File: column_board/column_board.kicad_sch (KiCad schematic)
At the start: 17 parts, among them J1 Bus_M.2_Socket_B, J10 USB_C_Receptacle_PowerOnly_6P, U1 CH32V30xRxTx, Y1 Crystal

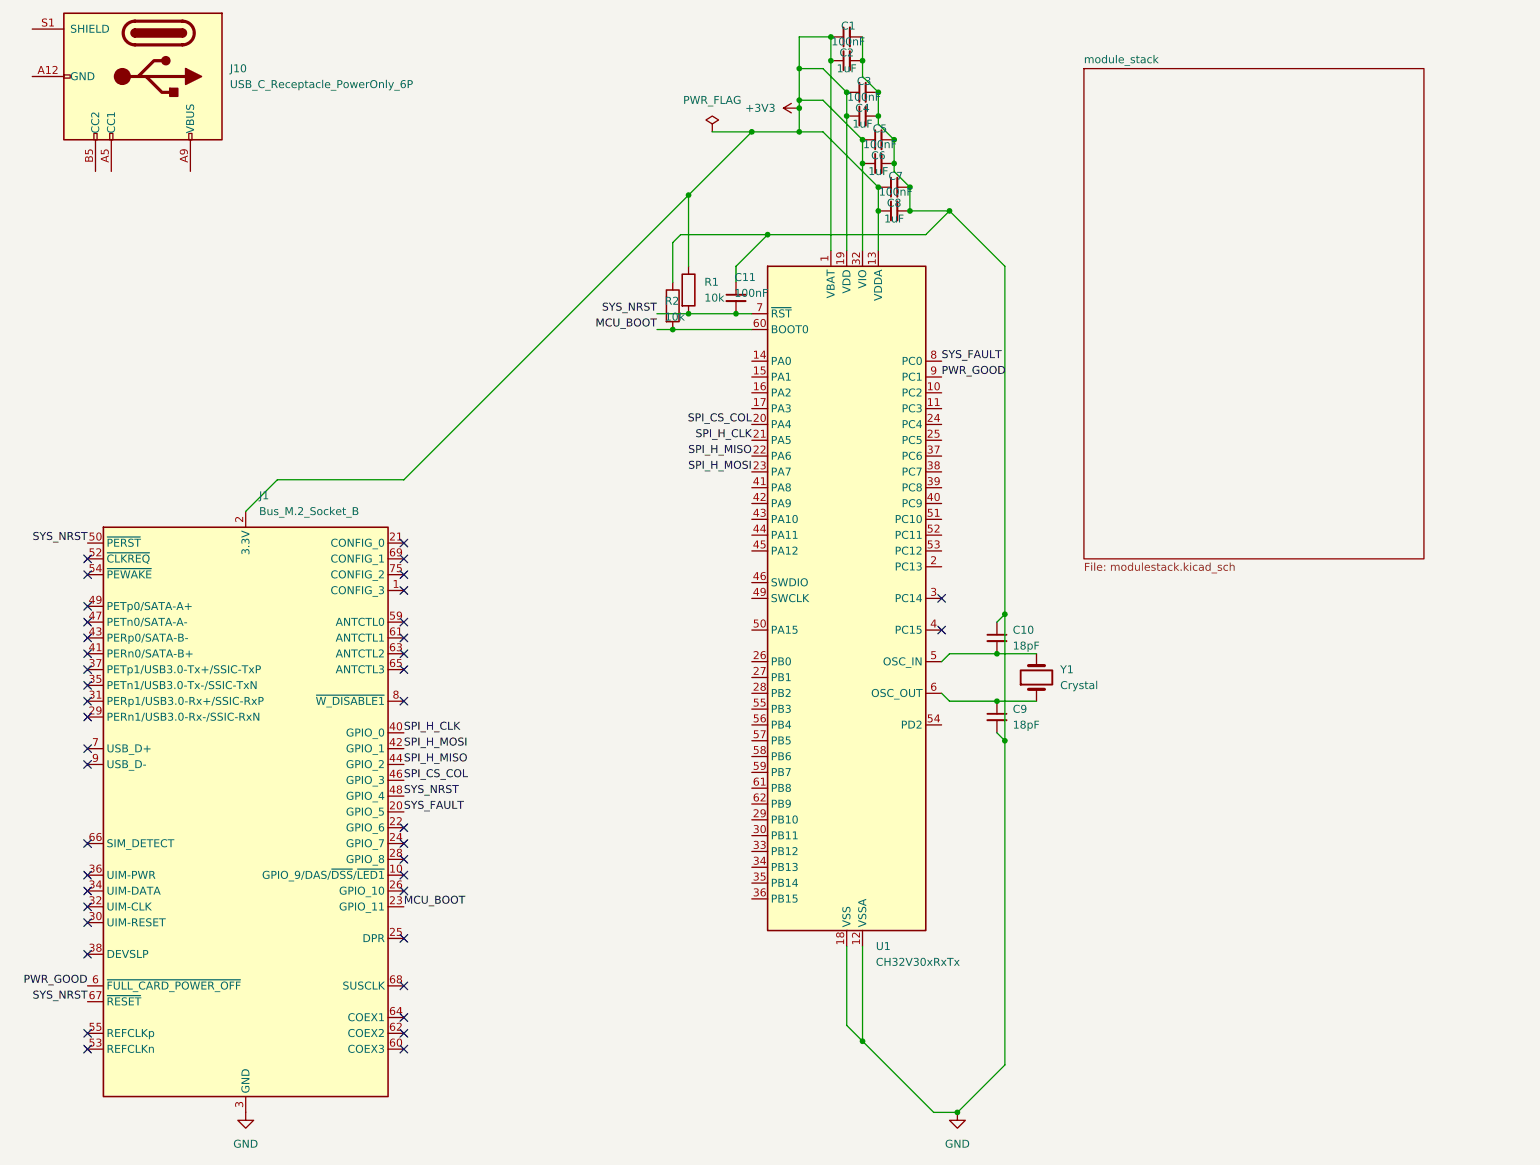
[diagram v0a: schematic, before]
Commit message: feat: create module connector system
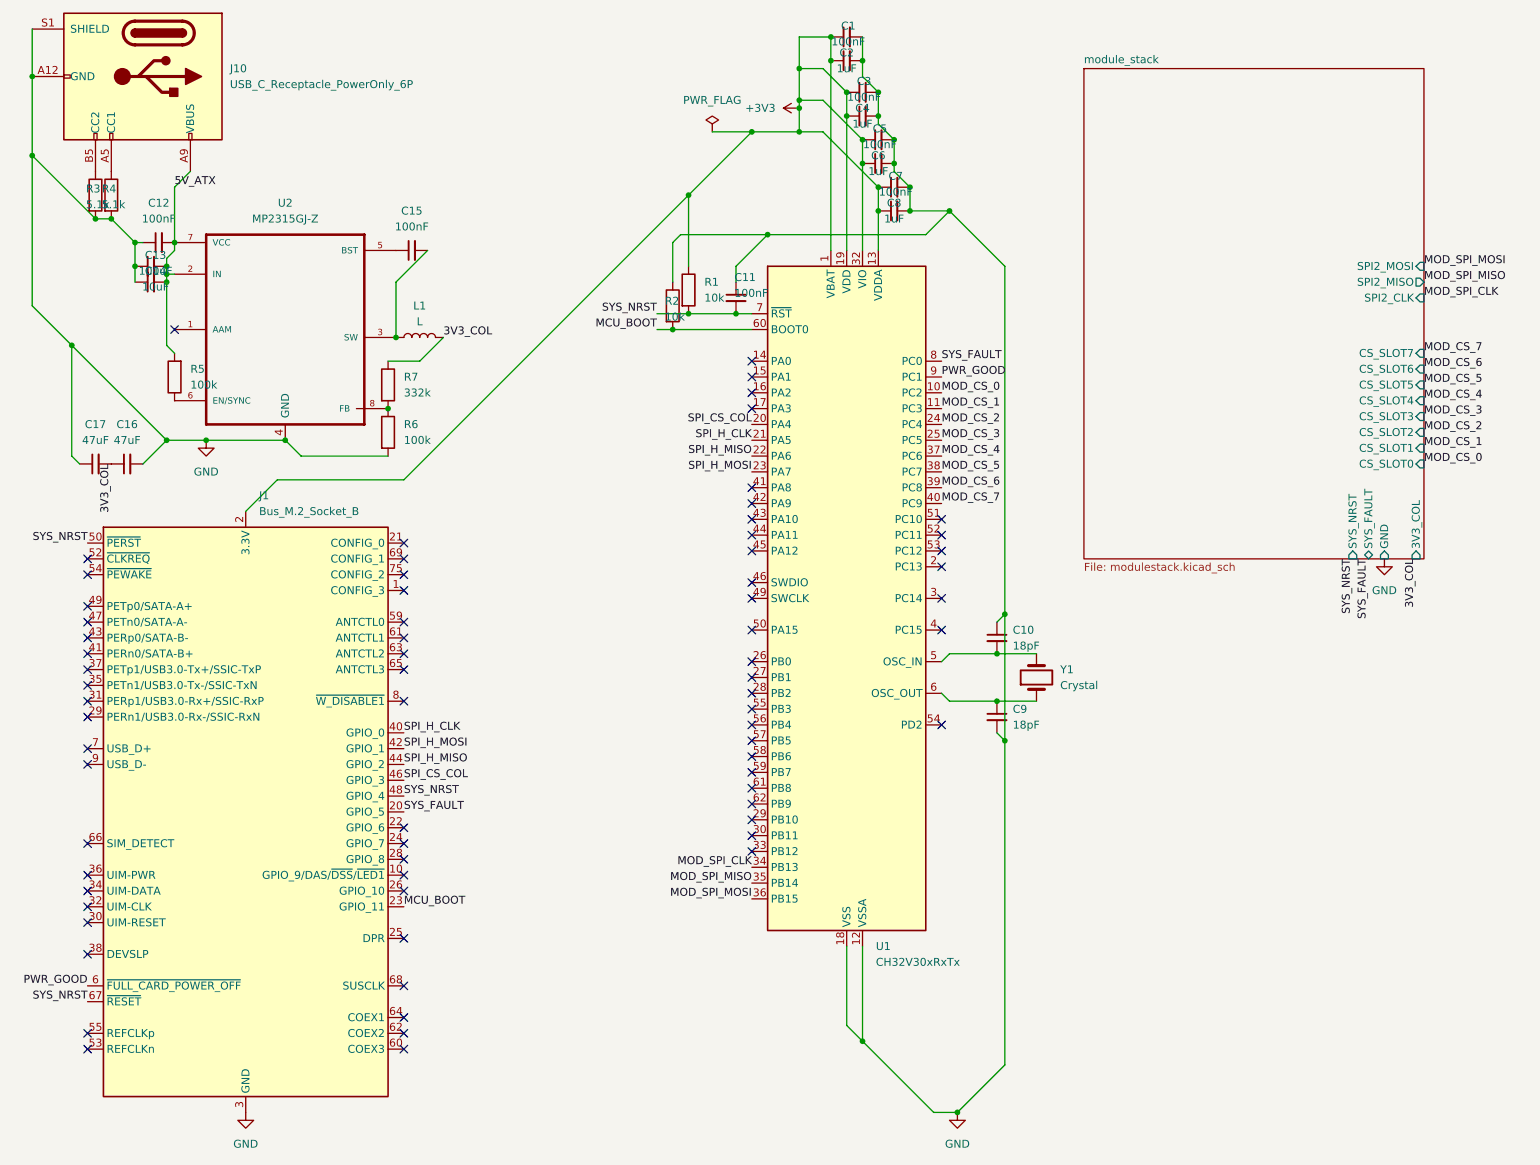
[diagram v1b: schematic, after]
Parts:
- added C12, C15: 100nF, symbol Device:C_Small
- added C13: 100uF, symbol Device:C_Small
- added C14: 10uF, symbol Device:C_Small
- added C16, C17: 47uF, symbol Device:C_Small
- added L1: L, symbol Device:L
- added R3, R4: 5.1k, symbol Device:R
- added R5, R6: 100k, symbol Device:R
- added R7: 332k, symbol Device:R
- added U2: MP2315GJ-Z, SOT65P280X100-8N, symbol MP2315GJ-Z:MP2315GJ-Z
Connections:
- net GND: now also J10.A12 (GND), J10.B12 (GND), J10.S1 (SHIELD), C12.1, C13.1, C14.1, C16.2, C17.1, R3.2, R4.2, R6.2, U2.4 (GND)
- net at J10.A5 (CC1): now also R4.1
- net 5V_ATX: now reaches J10.A9 (VBUS), J10.B9 (VBUS)
- net 5V_ATX: now also C12.2, C13.2, C14.2, R5.2, U2.2 (IN), U2.7 (VCC)
- net at J10.B5 (CC2): now also R3.1
- net MOD_CS_0: now reaches U1.10 (PC2)
- net MOD_CS_1: now reaches U1.11 (PC3)
- net MOD_CS_2: now reaches U1.24 (PC4)
- net MOD_CS_3: now reaches U1.25 (PC5)
- net MOD_SPI_CLK: now reaches U1.34 (PB13)
- net MOD_SPI_MISO: now reaches U1.35 (PB14)
- net MOD_SPI_MOSI: now reaches U1.36 (PB15)
- net MOD_CS_4: now reaches U1.37 (PC6)
- net MOD_CS_5: now reaches U1.38 (PC7)
- net MOD_CS_6: now reaches U1.39 (PC8)
- net MOD_CS_7: now reaches U1.40 (PC9)
- new net: R6.1, R7.2, U2.8 (FB)
- new net: C15.2, L1.1, U2.3 (SW)
- new net: R5.1, U2.6 (EN/SYNC)
- new net: C15.1, U2.5 (BST)
- new net 3V3_COL: C16.1, C17.2, L1.2, R7.1
- no-connect marks 41 -> 72
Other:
- sheet module_stack ports: added 3V3_COL, CS_SLOT0, CS_SLOT1, CS_SLOT2, CS_SLOT3, CS_SLOT4, CS_SLOT5, CS_SLOT6, CS_SLOT7, GND, SPI2_CLK, SPI2_MISO, SPI2_MOSI, SYS_FAULT, SYS_NRST; removed none
